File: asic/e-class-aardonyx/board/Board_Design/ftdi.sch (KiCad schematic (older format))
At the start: 62 parts, among them J1 USB_B_6PIN, J17 USB_OTG, J18 Conn_1x3_M, J2 Conn_1x8, J3 Conn_1x3_M, U1 FT2232H, U16 93LC56BT-I_OT, Y1 12MHz

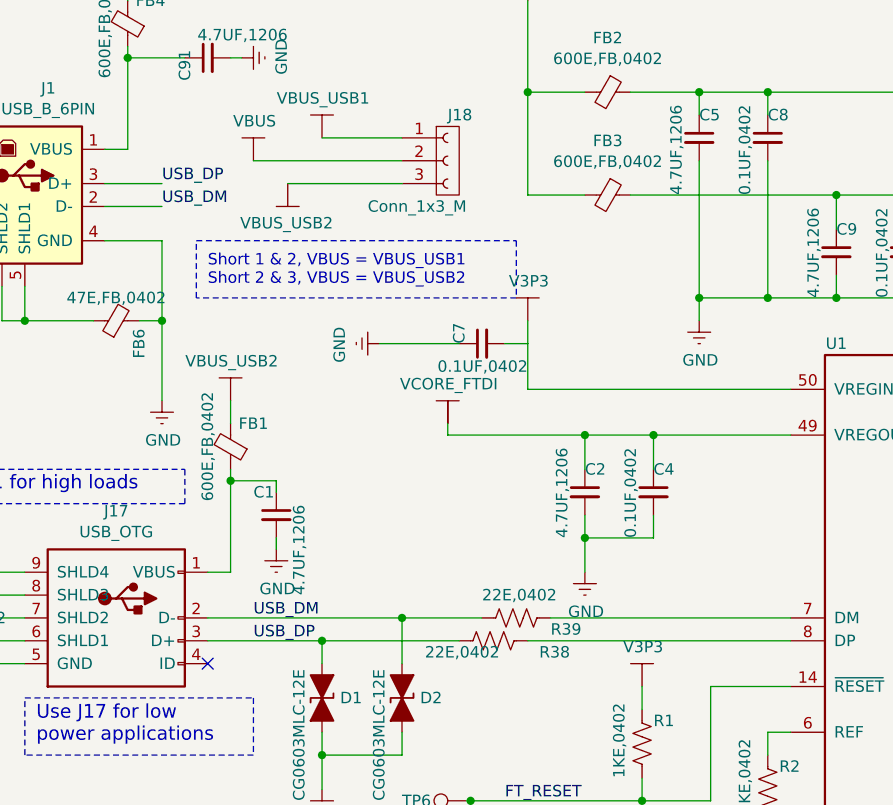
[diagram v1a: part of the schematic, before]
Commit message: update track & add the aardonyx project
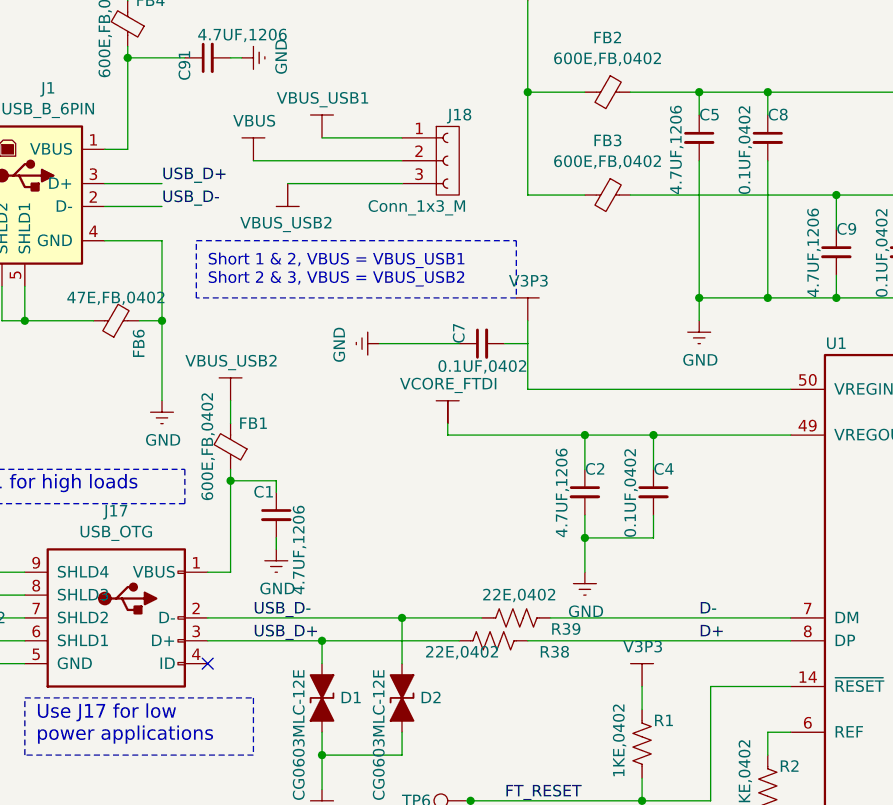
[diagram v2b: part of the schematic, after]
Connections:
- net D-: now reaches R39.1, U1.7 (DM)
- net D+: now reaches R38.1, U1.8 (DP)
- net USB_DM renamed USB_D-
- net USB_DP renamed USB_D+
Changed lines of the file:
@@
 Wire Wire Line
 	1100 2350 1000 2350
-Text Label 2100 3650 0    50   ~ 0
-USB_DM
-Text Label 2100 3750 0    50   ~ 0
-USB_DP
 Wire Wire Line
 	1550 1200 1800 1200
 Text Label 1700 1750 0    50   ~ 0
-USB_DP
+USB_D+
 Text Label 1700 1850 0    50   ~ 0
-USB_DM
+USB_D-
 $Comp
 L Aardonyx-rescue:Conn_1x3_M-aardonyx J?
@@
 Text Label 9300 3350 0    39   ~ 0
 TMS
+Text Label 4050 3750 0    50   ~ 0
+D+
+Text Label 4050 3650 0    50   ~ 0
+D-
+Text Label 2100 3750 0    50   ~ 0
+USB_D+
+Text Label 2100 3650 0    50   ~ 0
+USB_D-
 $EndSCHEMATC
